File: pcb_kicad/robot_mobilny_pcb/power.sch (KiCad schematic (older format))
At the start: 20 parts, among them J7 Power 14.8V, J8 STEP_DOWN_D24V50F5, Q1 IRF540N, SW2 SW_SPDT, U2 LF33_TO252

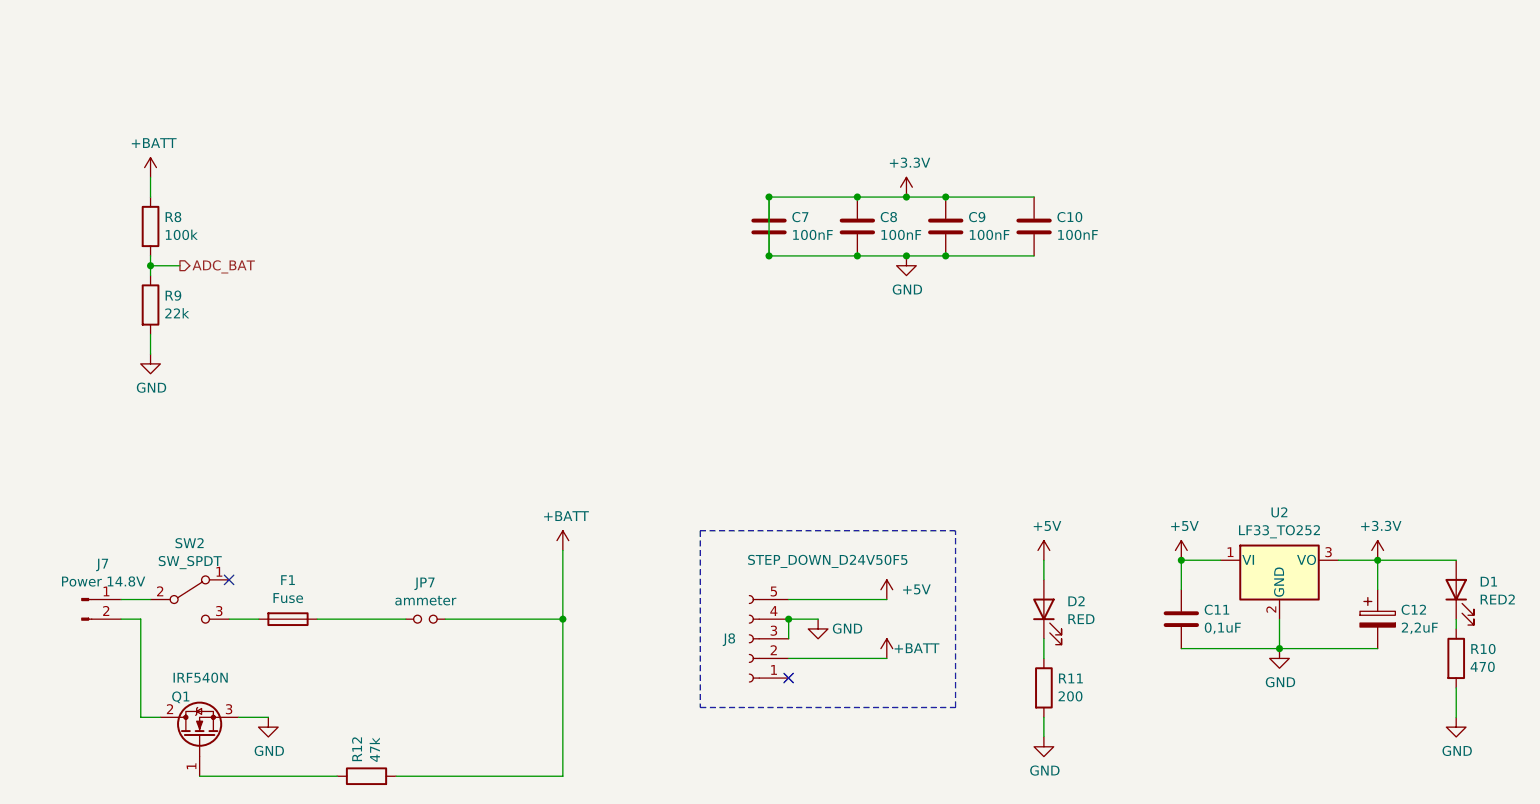
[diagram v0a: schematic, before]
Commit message: schematic update
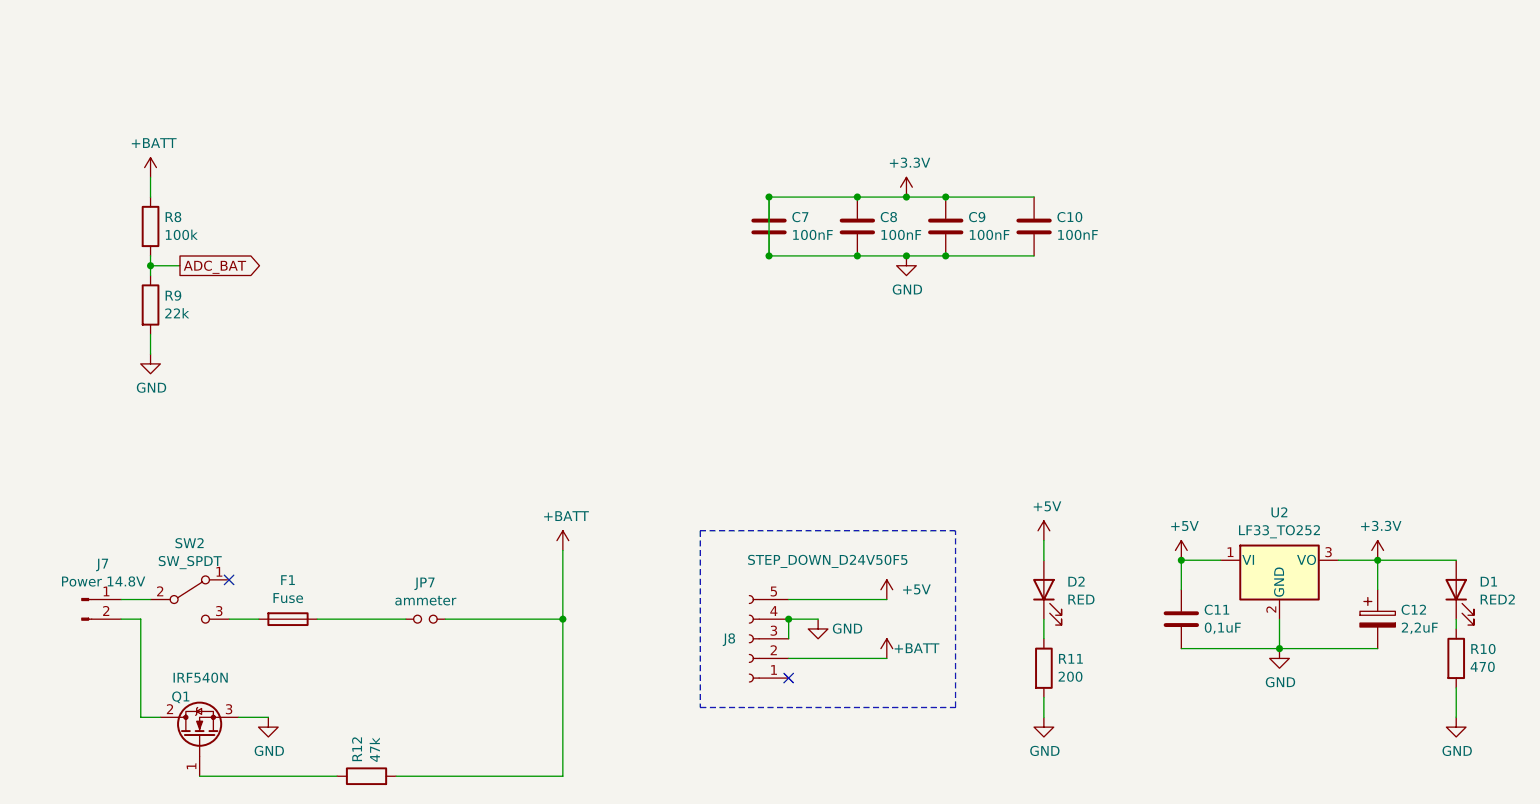
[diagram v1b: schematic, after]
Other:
- moved on the sheet: D2, R11
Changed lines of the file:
@@
 $Descr A4 11693 8268
 encoding utf-8
-Sheet 2 4
+Sheet 5 5
 Title "PCB robota mobilnego"
 Date "2021-10-21"
@@
 L power:+5V #PWR017
 U 1 1 6172E700
-P 7050 3800
-F 0 "#PWR017" H 7050 3650 50  0001 C CNN
-F 1 "+5V" H 7065 3973 50  0000 C CNN
-F 2 "" H 7050 3800 50  0001 C CNN
-F 3 "" H 7050 3800 50  0001 C CNN
-	1    7050 3800
+P 7050 3700
+F 0 "#PWR017" H 7050 3550 50  0001 C CNN
+F 1 "+5V" H 7065 3873 50  0000 C CNN
+F 2 "" H 7050 3700 50  0001 C CNN
+F 3 "" H 7050 3700 50  0001 C CNN
+	1    7050 3700
 	1    0    0    -1
 $EndComp
@@
 L Device:LED D2
 U 1 1 6174105C
-P 7050 4050
-F 0 "D2" V 7089 3932 50  0000 R CNN
-F 1 "RED" V 6998 3932 50  0000 R CNN
-F 2 "LED_THT:LED_D5.0mm" H 7050 4050 50  0001 C CNN
-F 3 "~" H 7050 4050 50  0001 C CNN
-	1    7050 4050
+P 7050 3950
+F 0 "D2" V 7089 3832 50  0000 R CNN
+F 1 "RED" V 6998 3832 50  0000 R CNN
+F 2 "LED_THT:LED_D5.0mm" H 7050 3950 50  0001 C CNN
+F 3 "~" H 7050 3950 50  0001 C CNN
+	1    7050 3950
 	0    -1   -1   0
 $EndComp
 Wire Wire Line
-	7050 3900 7050 3800
+	7050 3800 7050 3700
 $Comp
 L Device:R R11
 U 1 1 61744B32
-P 7050 4450
-F 0 "R11" H 7120 4496 50  0000 L CNN
-F 1 "200" H 7120 4405 50  0000 L CNN
-F 2 "" V 6980 4450 50  0001 C CNN
-F 3 "~" H 7050 4450 50  0001 C CNN
-	1    7050 4450
-	1    0    0    -1
-$EndComp
-Wire Wire Line
-	7050 4200 7050 4300
+P 7050 4350
+F 0 "R11" H 7120 4396 50  0000 L CNN
+F 1 "200" H 7120 4305 50  0000 L CNN
+F 2 "" V 6980 4350 50  0001 C CNN
+F 3 "~" H 7050 4350 50  0001 C CNN
+	1    7050 4350
+	1    0    0    -1
+$EndComp
+Wire Wire Line
+	7050 4100 7050 4200
 $Comp
 L power:GND #PWR026
 U 1 1 61745939
-P 7050 4700
-F 0 "#PWR026" H 7050 4450 50  0001 C CNN
-F 1 "GND" H 7055 4527 50  0000 C CNN
-F 2 "" H 7050 4700 50  0001 C CNN
-F 3 "" H 7050 4700 50  0001 C CNN
-	1    7050 4700
-	1    0    0    -1
-$EndComp
-Wire Wire Line
-	7050 4600 7050 4700
+P 7050 4600
+F 0 "#PWR026" H 7050 4350 50  0001 C CNN
+F 1 "GND" H 7055 4427 50  0000 C CNN
+F 2 "" H 7050 4600 50  0001 C CNN
+F 3 "" H 7050 4600 50  0001 C CNN
+	1    7050 4600
+	1    0    0    -1
+$EndComp
+Wire Wire Line
+	7050 4500 7050 4600
 $Comp
 L Device:Fuse F1
@@
 Wire Wire Line
 	6350 2250 6550 2250
-Text HLabel 2650 2300 2    50   Output ~ 0
-ADC_BAT
 $Comp
 L Device:R R8
@@
 Wire Wire Line
 	3350 4100 3800 4100
+Text GLabel 2650 2300 2    50   Output ~ 0
+ADC_BAT
 $EndSCHEMATC

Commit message: schematic_update
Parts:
- removed F1: Fuse, symbol Device:Fuse
- C1: renamed from C7; footprint (none) -> Capacitor_THT:C_Disc_D5.0mm_W2.5mm_P2.50mm
- C2: renamed from C8; footprint (none) -> Capacitor_THT:C_Disc_D5.0mm_W2.5mm_P2.50mm
- C3: renamed from C9; footprint (none) -> Capacitor_THT:C_Disc_D5.0mm_W2.5mm_P2.50mm
- C4: renamed from C10; footprint (none) -> Capacitor_THT:C_Disc_D5.0mm_W2.5mm_P2.50mm
- C5: renamed from C11; value 0,1uF -> 100nF; footprint (none) -> Capacitor_THT:C_Disc_D5.0mm_W2.5mm_P2.50mm
- C6: renamed from C12; footprint (none) -> Capacitor_THT:CP_Radial_D4.0mm_P1.50mm
- R1: renamed from R8; footprint (none) -> Resistor_THT:R_Axial_DIN0207_L6.3mm_D2.5mm_P10.16mm_Horizontal
- R3: renamed from R10; footprint (none) -> Resistor_THT:R_Axial_DIN0207_L6.3mm_D2.5mm_P10.16mm_Horizontal
- R4: renamed from R11; value 200 -> 470; footprint (none) -> Resistor_THT:R_Axial_DIN0207_L6.3mm_D2.5mm_P10.16mm_Horizontal
- R5: renamed from R12; footprint (none) -> Resistor_THT:R_Axial_DIN0207_L6.3mm_D2.5mm_P10.16mm_Horizontal
- SW1: renamed from SW2; footprint (none) -> Button_Switch_THT:SW_CuK_JS202011CQN_DPDT_Straight
- renumbered D2 to D1, D1 to D2, J7 to J1, J8 to J2, JP7 to JP1, R9 to R2, U2 to U1
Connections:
- net +3V3: no longer C1.2, C2.2, C3.2, C4.2, C5.2, C6.2, J2.3 (Pin_3), J2.4 (Pin_4), Q1.3 (S), R2.2, R3.2, R4.2, U1.2 (GND)
- net at SW1.3 (C): now also JP1.1
- new net GND: C1.2, C2.2, C3.2, C4.2, C5.2, C6.2, J2.3 (Pin_3), J2.4 (Pin_4), Q1.3 (S), R2.2, R3.2, R4.2, U1.2 (GND)

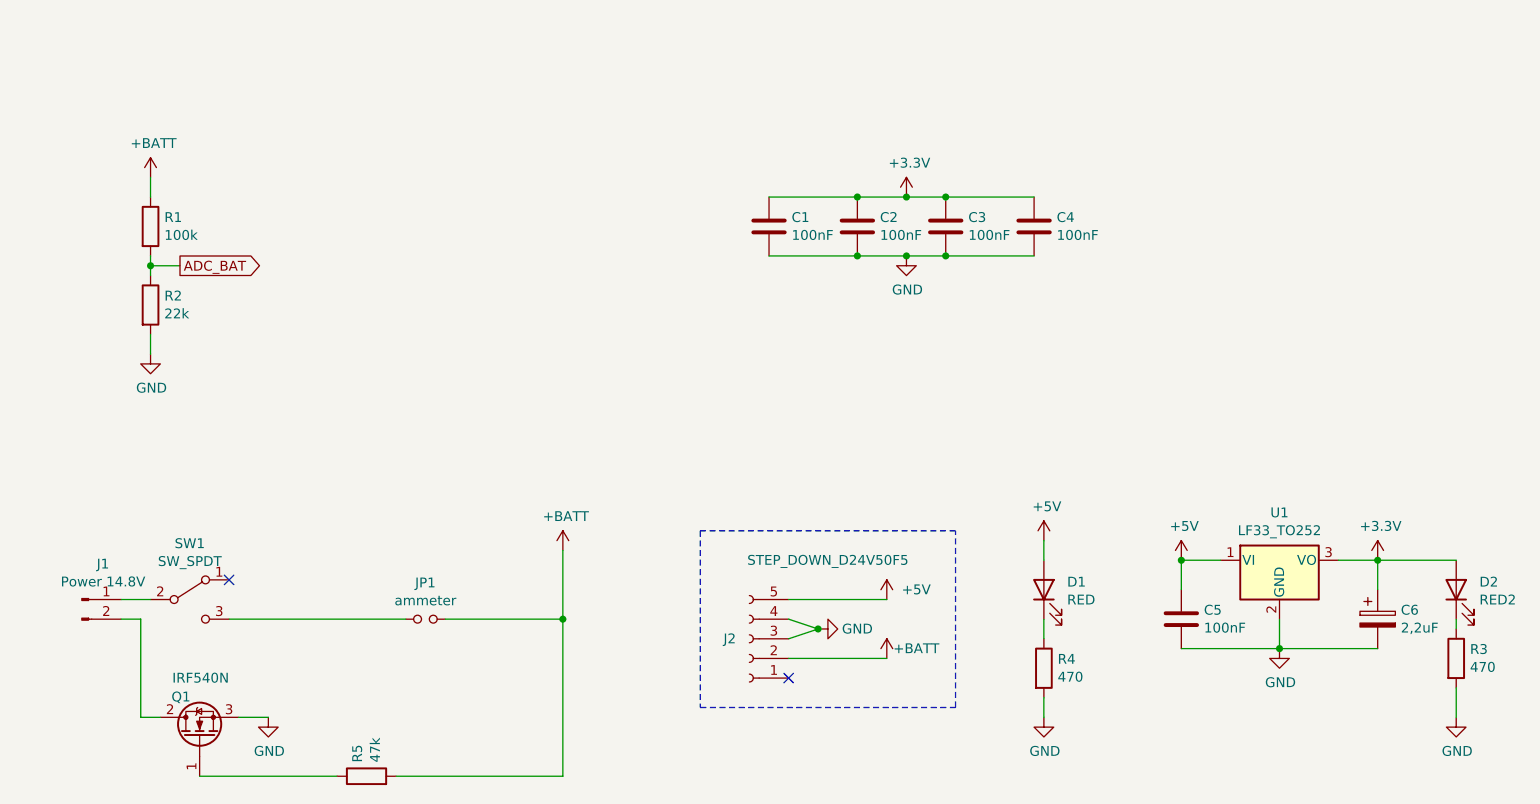
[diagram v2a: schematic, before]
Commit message: PCB_update
Change of  motor controller connector to Arduino shields
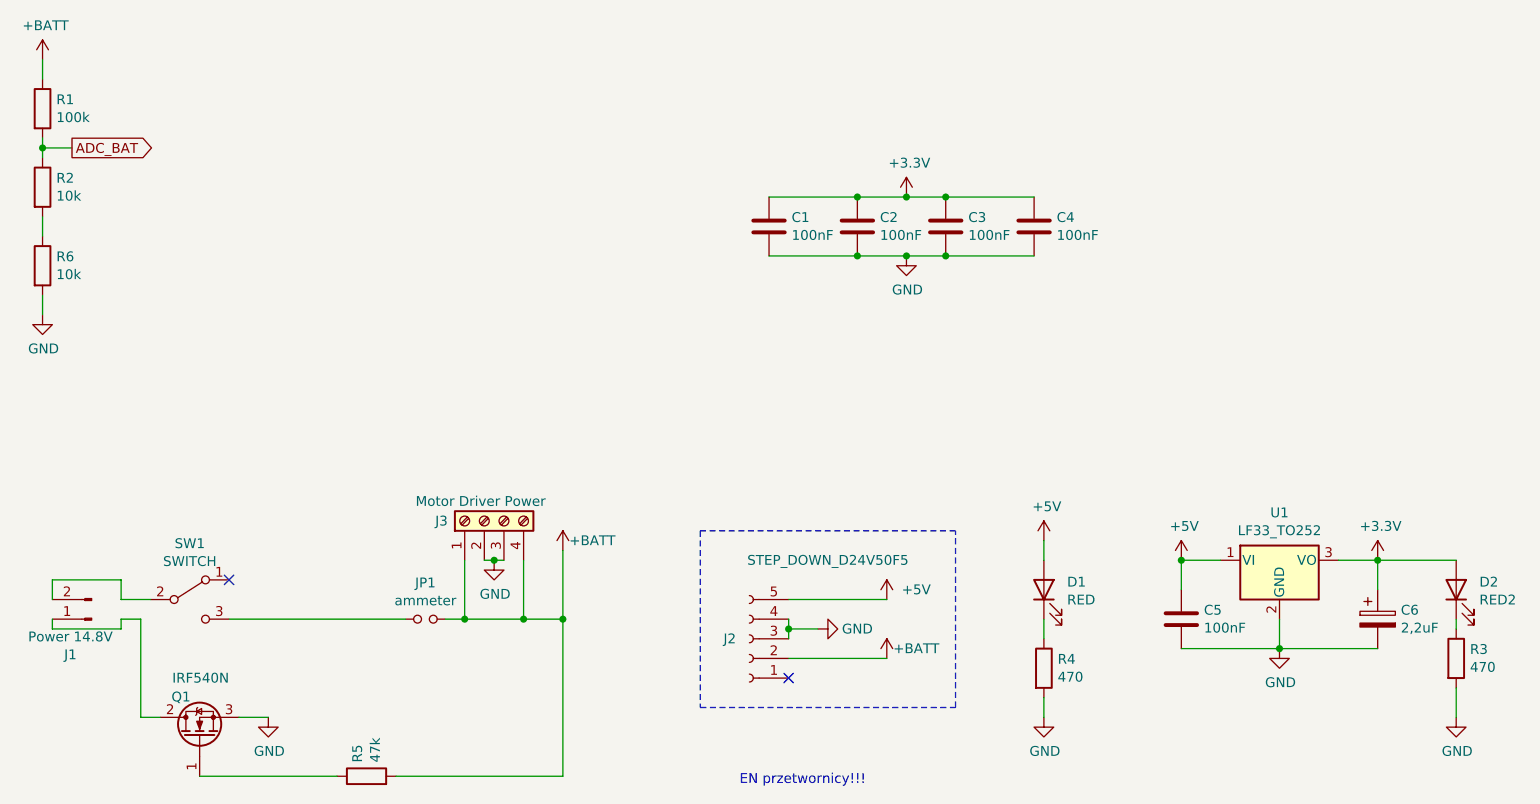
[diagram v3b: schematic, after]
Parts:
- added J3: Motor Driver Power, TerminalBlock_Phoenix:TerminalBlock_Phoenix_MKDS-1,5-4_1x04_P5.00mm_Horizontal, symbol Connector:Screw_Terminal_01x04
- added R6: 10k, Resistor_THT:R_Axial_DIN0207_L6.3mm_D2.5mm_P10.16mm_Horizontal, symbol Device:R
- R2: value 22k -> 10k; footprint (none) -> Resistor_THT:R_Axial_DIN0207_L6.3mm_D2.5mm_P10.16mm_Horizontal
- SW1: value SW_SPDT -> SWITCH
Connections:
- net +BATT: now also J3.1 (Pin_1), J3.4 (Pin_4)
- net GND: now also J3.2 (Pin_2), J3.3 (Pin_3), R6.2; no longer R2.2
- net at J1.1 (Pin_1): now also Q1.2 (D); no longer SW1.2 (B)
- net at J1.2 (Pin_2): now also SW1.2 (B); no longer Q1.2 (D)
- new net: R2.2, R6.1
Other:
- note added: "EN przetwornicy!!!\n"
- moved on the sheet: J1, R1, R2
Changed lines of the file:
@@
 L Connector:Conn_01x02_Male J1
 U 1 1 61721F49
-P 2150 4000
-F 0 "J1" H 2258 4181 50  0000 C CNN
-F 1 "Power 14.8V" H 2258 4090 50  0000 C CNN
-F 2 "Connector_AMASS:AMASS_XT60-M_1x02_P7.20mm_Vertical" H 2150 4000 50  0001 C CNN
-F 3 "~" H 2150 4000 50  0001 C CNN
-	1    2150 4000
-	1    0    0    -1
+P 2200 4100
+F 0 "J1" H 2308 4281 50  0000 C CNN
+F 1 "Power 14.8V" H 2308 4190 50  0000 C CNN
+F 2 "Connector_AMASS:AMASS_XT60-M_1x02_P7.20mm_Vertical" H 2200 4100 50  0001 C CNN
+F 3 "~" H 2200 4100 50  0001 C CNN
+	1    2200 4100
+	-1   0    0    1
 $EndComp
 $Comp
@@
 P 2700 4000
 F 0 "SW1" H 2700 4285 50  0000 C CNN
-F 1 "SW_SPDT" H 2700 4194 50  0000 C CNN
+F 1 "SWITCH" H 2700 4194 50  0000 C CNN
 F 2 "Button_Switch_THT:SW_CuK_JS202011CQN_DPDT_Straight" H 2700 4000 50  0001 C CNN
 F 3 "~" H 2700 4000 50  0001 C CNN
@@
 L Device:R R1
 U 1 1 617FFF5E
-P 2500 2100
-F 0 "R1" H 2570 2146 50  0000 L CNN
-F 1 "100k" H 2570 2055 50  0000 L CNN
-F 2 "Resistor_THT:R_Axial_DIN0207_L6.3mm_D2.5mm_P10.16mm_Horizontal" V 2430 2100 50  0001 C CNN
-F 3 "~" H 2500 2100 50  0001 C CNN
-	1    2500 2100
+P 1950 1500
+F 0 "R1" H 2020 1546 50  0000 L CNN
+F 1 "100k" H 2020 1455 50  0000 L CNN
+F 2 "Resistor_THT:R_Axial_DIN0207_L6.3mm_D2.5mm_P10.16mm_Horizontal" V 1880 1500 50  0001 C CNN
+F 3 "~" H 1950 1500 50  0001 C CNN
+	1    1950 1500
 	1    0    0    -1
 $EndComp
@@
 L Device:R R2
 U 1 1 6180038E
-P 2500 2500
-F 0 "R2" H 2570 2546 50  0000 L CNN
-F 1 "22k" H 2570 2455 50  0000 L CNN
-F 2 "" V 2430 2500 50  0001 C CNN
-F 3 "~" H 2500 2500 50  0001 C CNN
-	1    2500 2500
-	1    0    0    -1
-$EndComp
-Wire Wire Line
-	2500 2250 2500 2300
-Wire Wire Line
-	2500 2300 2650 2300
-Connection ~ 2500 2300
-Wire Wire Line
-	2500 2300 2500 2350
+P 1950 1900
+F 0 "R2" H 2020 1946 50  0000 L CNN
+F 1 "10k" H 2020 1855 50  0000 L CNN
+F 2 "Resistor_THT:R_Axial_DIN0207_L6.3mm_D2.5mm_P10.16mm_Horizontal" V 1880 1900 50  0001 C CNN
+F 3 "~" H 1950 1900 50  0001 C CNN
+	1    1950 1900
+	1    0    0    -1
+$EndComp
+Wire Wire Line
+	1950 1650 1950 1700
+Wire Wire Line
+	1950 1700 2100 1700
+Connection ~ 1950 1700
+Wire Wire Line
+	1950 1700 1950 1750
 $Comp
 L power:GND #PWR04
 U 1 1 618024FC
-P 2500 2750
-F 0 "#PWR04" H 2500 2500 50  0001 C CNN
-F 1 "GND" H 2505 2577 50  0000 C CNN
-F 2 "" H 2500 2750 50  0001 C CNN
-F 3 "" H 2500 2750 50  0001 C CNN
-	1    2500 2750
-	1    0    0    -1
-$EndComp
-Wire Wire Line
-	2500 2750 2500 2650
+P 1950 2550
+F 0 "#PWR04" H 1950 2300 50  0001 C CNN
+F 1 "GND" H 1955 2377 50  0000 C CNN
+F 2 "" H 1950 2550 50  0001 C CNN
+F 3 "" H 1950 2550 50  0001 C CNN
+	1    1950 2550
+	1    0    0    -1
+$EndComp
+Wire Wire Line
+	1950 2150 1950 2050
 $Comp
 L power:+BATT #PWR01
 U 1 1 61805B4F
-P 2500 1850
-F 0 "#PWR01" H 2500 1700 50  0001 C CNN
-F 1 "+BATT" H 2515 2023 50  0000 C CNN
-F 2 "" H 2500 1850 50  0001 C CNN
-F 3 "" H 2500 1850 50  0001 C CNN
-	1    2500 1850
+P 1950 1250
+F 0 "#PWR01" H 1950 1100 50  0001 C CNN
+F 1 "+BATT" H 1965 1423 50  0000 C CNN
+F 2 "" H 1950 1250 50  0001 C CNN
+F 3 "" H 1950 1250 50  0001 C CNN
+	1    1950 1250
 	1    0    0    -1
 $EndComp
@@
 P 4600 3750
 F 0 "#PWR06" H 4600 3600 50  0001 C CNN
-F 1 "+BATT" H 4615 3923 50  0000 C CNN
+F 1 "+BATT" H 4750 3800 50  0000 C CNN
 F 2 "" H 4600 3750 50  0001 C CNN
 F 3 "" H 4600 3750 50  0001 C CNN
@@
 	8750 3800 9150 3800
 Wire Wire Line
-	2500 1850 2500 1950
+	1950 1250 1950 1350
 $Comp
 L Transistor_FET:IRF540N Q1
@@
 $EndComp
 Wire Wire Line
-	4000 4100 4600 4100
-Text GLabel 2650 2300 2    50   Output ~ 0
+	4000 4100 4100 4100
+Text GLabel 2100 1700 2    50   Output ~ 0
 ADC_BAT
-Wire Wire Line
-	5750 4100 5900 4150
-Wire Wire Line
-	5750 4200 5900 4150
-Connection ~ 5900 4150
 $Comp
 L power:GND #PWR013
@@
 $EndComp
 NoConn ~ 2900 3900
+$Comp
+L Device:R R6
+U 1 1 61C22DF9
+P 1950 2300
+F 0 "R6" H 2020 2346 50  0000 L CNN
+F 1 "10k" H 2020 2255 50  0000 L CNN
+F 2 "Resistor_THT:R_Axial_DIN0207_L6.3mm_D2.5mm_P10.16mm_Horizontal" V 1880 2300 50  0001 C CNN
+F 3 "~" H 1950 2300 50  0001 C CNN
+	1    1950 2300
+	1    0    0    -1
+$EndComp
+Wire Wire Line
+	1950 2550 1950 2450
+$Comp
+L Connector:Screw_Terminal_01x04 J3
+U 1 1 61C7CD44
+P 4200 3600
+F 0 "J3" V 4200 3850 50  0000 R CNN
+F 1 "Motor Driver Power" V 4300 3950 50  0000 R CNN
+F 2 "TerminalBlock_Phoenix:TerminalBlock_Phoenix_MKDS-1,5-4_1x04_P5.00mm_Horizontal" H 4200 3600 50  0001 C CNN
+F 3 "~" H 4200 3600 50  0001 C CNN
+	1    4200 3600
+	0    -1   -1   0
+$EndComp
+Wire Wire Line
+	4100 3800 4100 4100
+Wire Wire Line
+	4400 3800 4400 4100
+Wire Wire Line
+	4200 3800 4250 3800
+$Comp
+L power:GND #PWR0119
+U 1 1 61C8004C
+P 4250 3800
+F 0 "#PWR0119" H 4250 3550 50  0001 C CNN
+F 1 "GND" H 4255 3627 50  0000 C CNN
+F 2 "" H 4250 3800 50  0001 C CNN
+F 3 "" H 4250 3800 50  0001 C CNN
+	1    4250 3800
+	1    0    0    -1
+$EndComp
+Connection ~ 4250 3800
+Wire Wire Line
+	4250 3800 4300 3800
+Wire Wire Line
+	5750 4100 5750 4150
+Wire Wire Line
+	5750 4150 5900 4150
+Connection ~ 5750 4150
+Wire Wire Line
+	5750 4150 5750 4200
+Wire Wire Line
+	2350 4000 2350 3900
+Wire Wire Line
+	2350 3900 2000 3900
+Wire Wire Line
+	2000 3900 2000 4000
+Wire Wire Line
+	2000 4100 2000 4150
+Wire Wire Line
+	2000 4150 2350 4150
+Wire Wire Line
+	2350 4150 2350 4100
+Connection ~ 4100 4100
+Wire Wire Line
+	4100 4100 4400 4100
+Connection ~ 4400 4100
+Wire Wire Line
+	4400 4100 4600 4100
 Wire Wire Line
 	2900 4100 3800 4100
+Text Notes 5500 4950 0    50   ~ 0
+EN przetwornicy!!!\n
 $EndSCHEMATC
